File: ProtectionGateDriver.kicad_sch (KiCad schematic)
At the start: 17 parts, among them J1 XT60_WHEEL, J2 12V_GATE_SUPPLY, Q1 MCTL1D0N08Y, U1 1EDN7550B

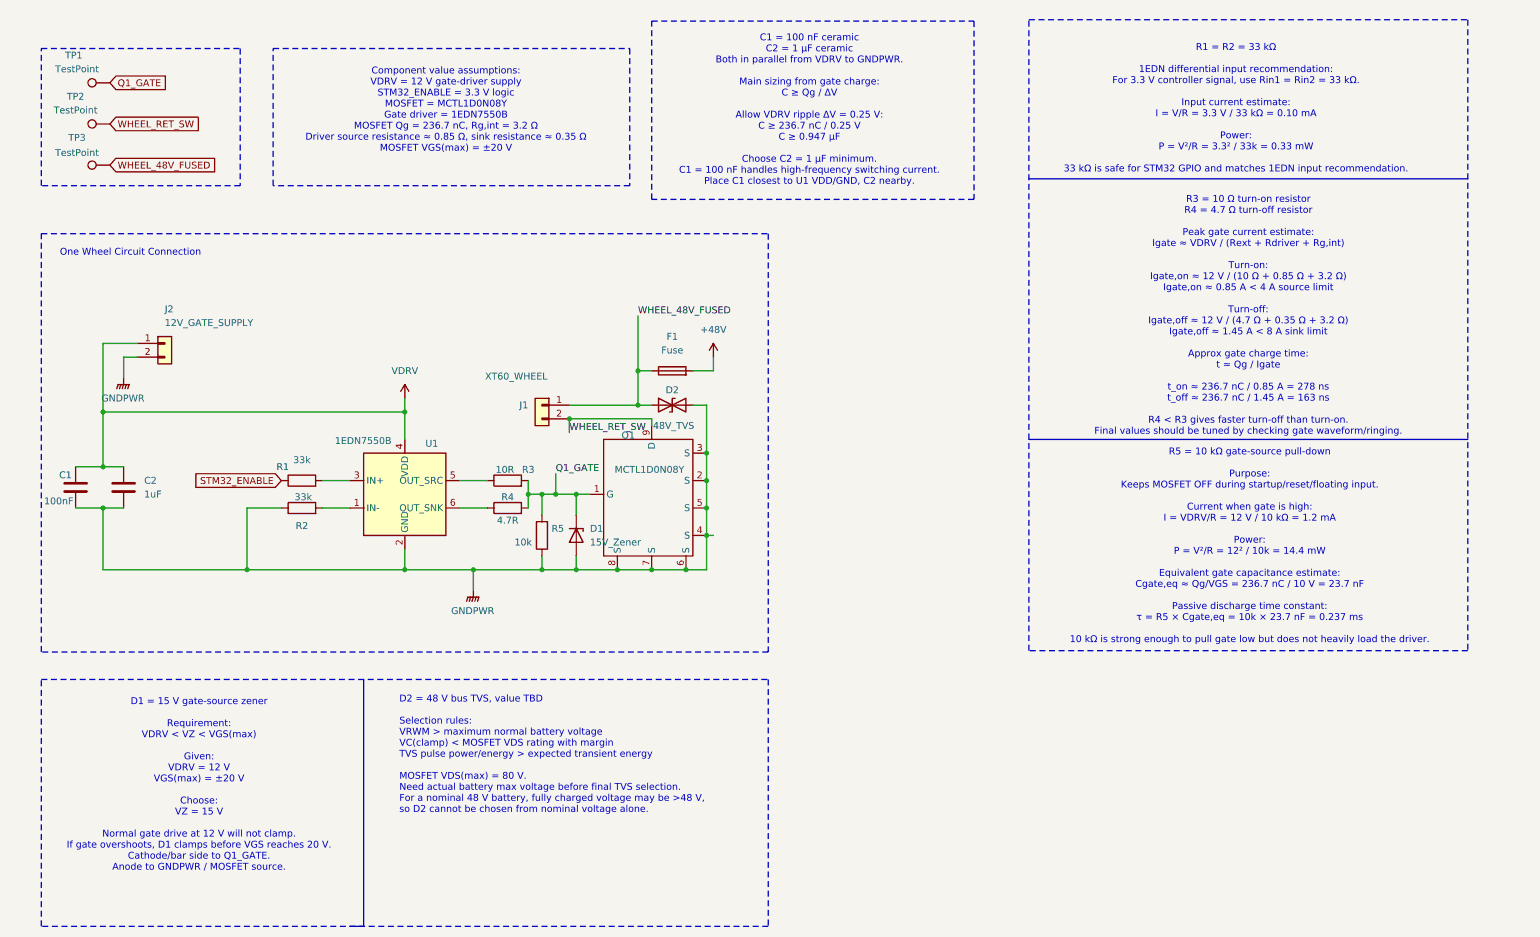
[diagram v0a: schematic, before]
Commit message: Sync approved one-wheel schematic and portable KiCad project for layout
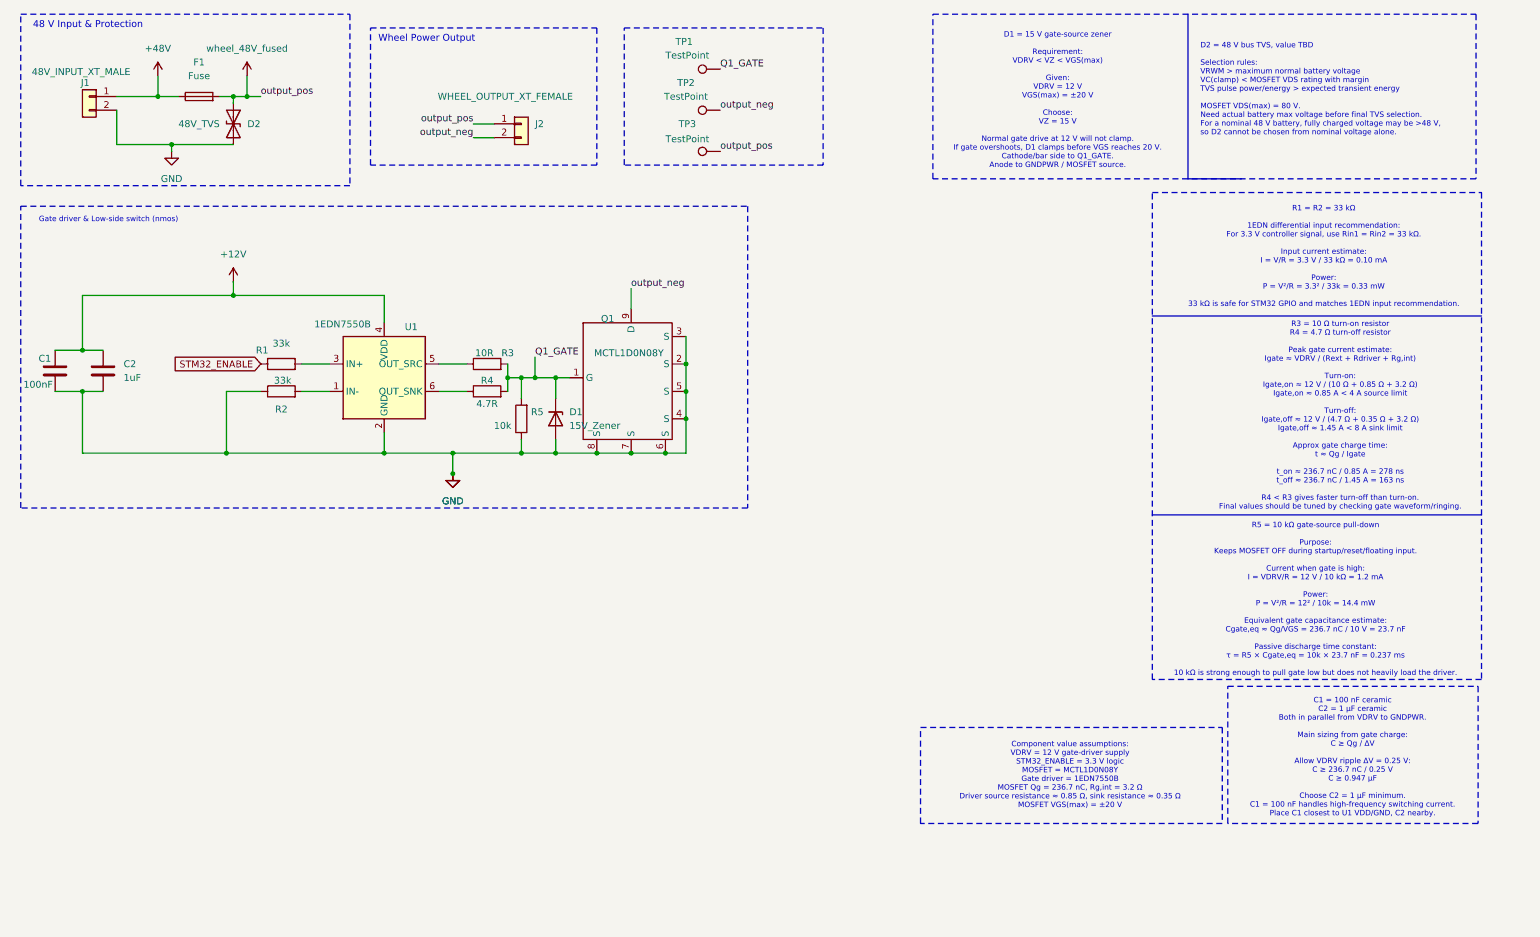
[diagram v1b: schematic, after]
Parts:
- removed J2: 12V_GATE_SUPPLY, symbol Connector_Generic:Conn_01x02
- added J1: 48V_INPUT_XT_MALE, symbol Connector_Generic:Conn_01x02
- J2: renamed from J1; value XT60_WHEEL -> WHEEL_OUTPUT_XT_FEMALE
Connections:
- net +48V: now also F1.1, J1.1 (Pin_1); no longer F1.2
- net GNDPWR renamed GND
- net GND: now also J1.2 (Pin_2)
- net VDRV renamed +12V
- net WHEEL_48V_FUSED renamed wheel_48V_fused
- net wheel_48V_fused: now also F1.2; no longer F1.1
- net WHEEL_RET_SW renamed output_neg
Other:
- note added: "48 V Input & Protection"
- note added: "Gate driver & Low-side switch (nmos)"
- note added: "Wheel Power Output"
- note removed: "One Wheel Circuit Connection"
- moved on the sheet: C1, C2, D1, D2, F1, J2, Q1, R1, R2, R3, R4, R5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

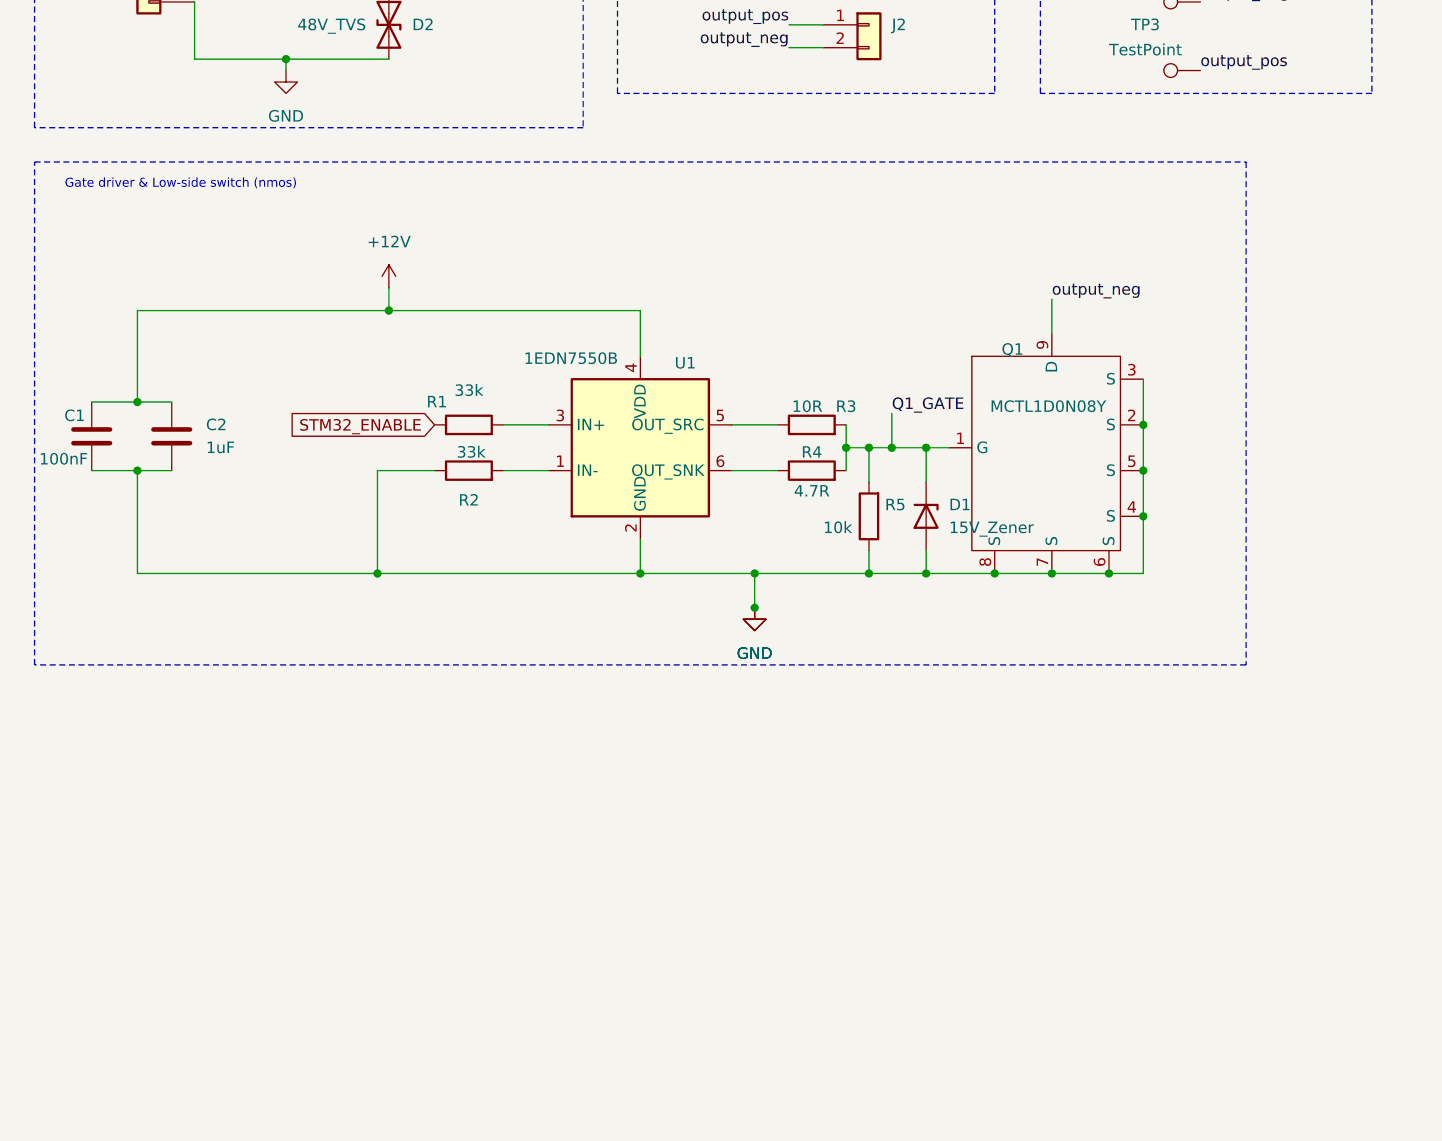
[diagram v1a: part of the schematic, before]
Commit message: Save connector and footprint assignments with initial unrouted PCB
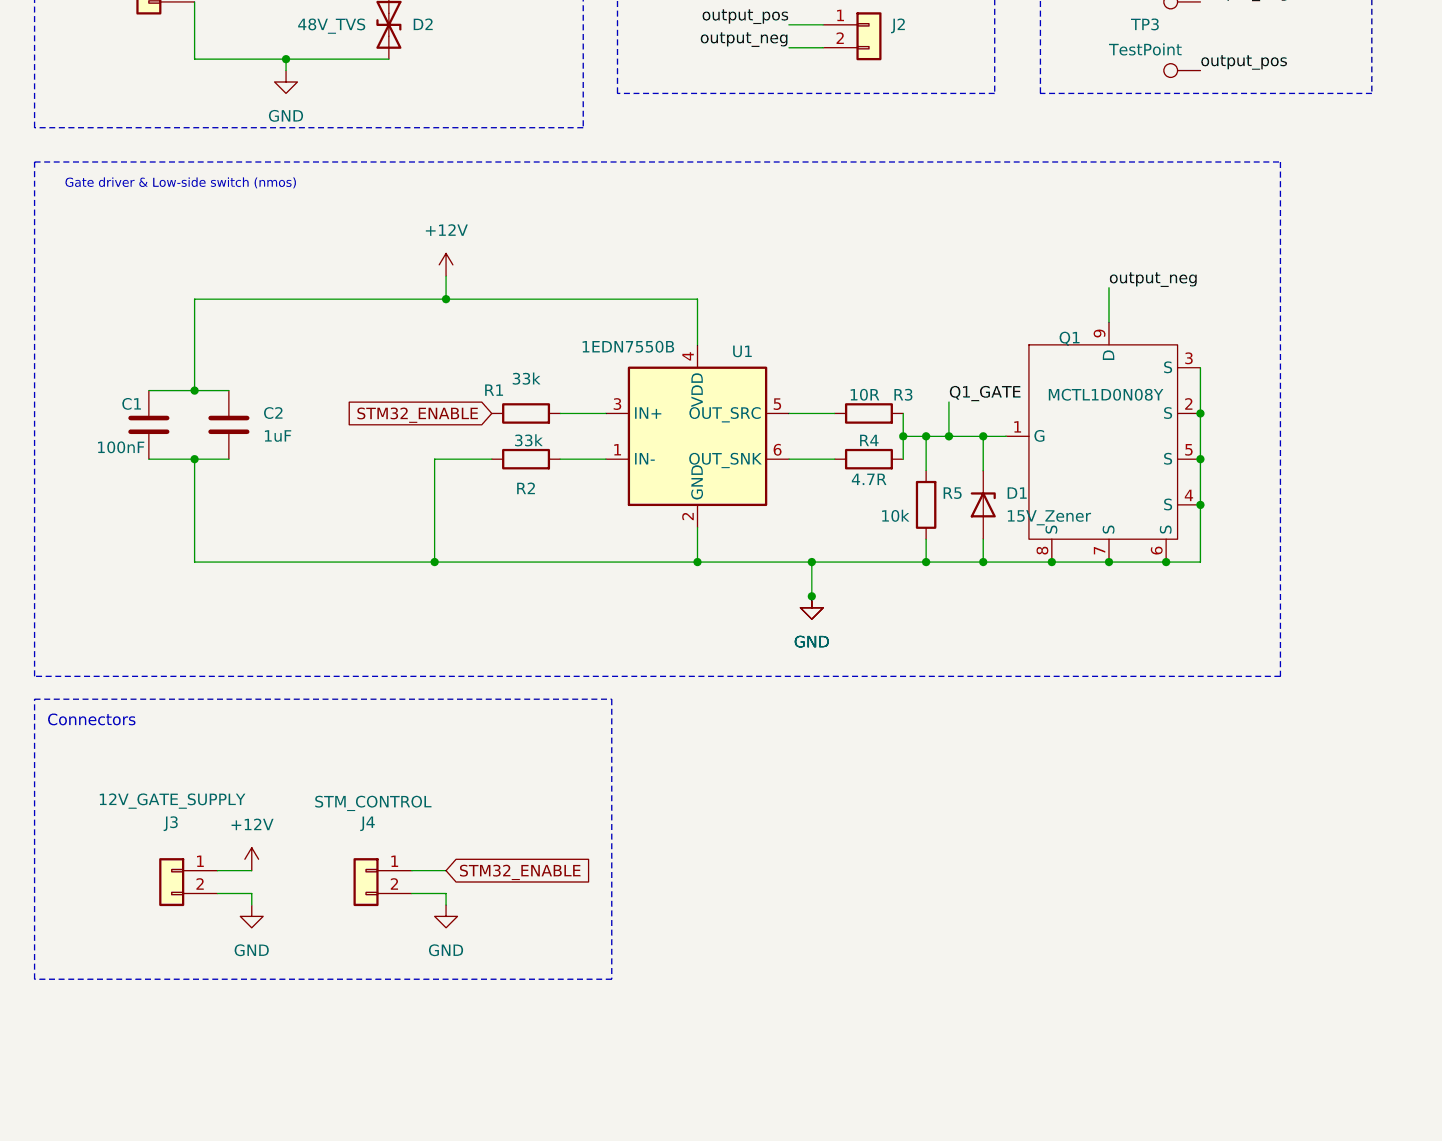
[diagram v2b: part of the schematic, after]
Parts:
- added J3: 12V_GATE_SUPPLY, Connector_JST:JST_XH_B2B-XH-A_1x02_P2.50mm_Vertical, symbol Connector_Generic:Conn_01x02
- added J4: STM_CONTROL, Connector_PinHeader_2.54mm:PinHeader_1x02_P2.54mm_Vertical, symbol Connector_Generic:Conn_01x02
- C1, C2: footprint (none) -> Capacitor_SMD:C_0805_2012Metric
- D1: footprint (none) -> Diode_SMD:D_SOD-123
- D2: footprint (none) -> Diode_SMD:D_SMB
- F1: footprint (none) -> Fuse:Fuseholder_Blade_Mini_Keystone_3568
- J1: footprint (none) -> Connector_AMASS:AMASS_XT60-M_1x02_P7.20mm_Vertical
- J2: footprint (none) -> Connector_AMASS:AMASS_XT60-F_1x02_P7.20mm_Vertical
- R1, R2, R3, R4, R5: footprint (none) -> Resistor_SMD:R_0805_2012Metric
- TP1, TP2, TP3: footprint (none) -> TestPoint:TestPoint_Pad_D2.0mm
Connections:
- net +12V: now also J3.1 (Pin_1)
- net GND: now also J3.2 (Pin_2), J4.2 (Pin_2)
- net STM32_ENABLE: now also J4.1 (Pin_1)
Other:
- note added: "Connectors"
- moved on the sheet: C1, C2, D1, Q1, R1, R2, R3, R4, R5, U1

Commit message: Correct iteration 2 native KiCad files from uploaded project
Replace stale PCB, project and schematic with the supplied iteration 2 files. Four-layer layout is a review checkpoint, not for fabrication.
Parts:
- TP1, TP2, TP3: footprint TestPoint:TestPoint_Pad_D2.0mm -> TestPoint:TestPoint_Pad_D1.0mm
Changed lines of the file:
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@@
 			)
 		)
-		(property "Footprint" "TestPoint:TestPoint_Pad_D2.0mm"
+		(property "Footprint" "TestPoint:TestPoint_Pad_D1.0mm"
 			(at 143.51 20.32 0)
 			(effects
@@
 			)
 		)
-		(property "Footprint" "TestPoint:TestPoint_Pad_D2.0mm"
+		(property "Footprint" "TestPoint:TestPoint_Pad_D1.0mm"
 			(at 143.51 27.94 0)
 			(effects
@@
 			)
 		)
-		(property "Footprint" "TestPoint:TestPoint_Pad_D2.0mm"
+		(property "Footprint" "TestPoint:TestPoint_Pad_D1.0mm"
 			(at 143.51 35.56 0)
 			(effects

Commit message: Save third protection-board layout iteration with native KiCad files
Add input capacitor, M2 mounting holes, rounded outline and updated screenshots. Development checkpoint only; not for fabrication.
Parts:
- added C3: 1uF, Capacitor_THT:C_Rect_L13.0mm_W8.0mm_P10.00mm_FKS3_FKP3_MKS4, symbol Device:C
- added H1, H2, H3, H4: MountingHole, MountingHole:MountingHole_2.2mm_M2, symbol Mechanical:MountingHole
- added TP4: TestPoint, TestPoint:TestPoint_Pad_D1.0mm, symbol Connector:TestPoint
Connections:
- net GND: now also C3.2, TP4.1
- net wheel_48V_fused: now also C3.1
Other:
- note added: "Mounting Holes"
- moved on the sheet: TP1, TP2, TP3
